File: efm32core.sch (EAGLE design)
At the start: 53 parts, among them U1 IP4220CZ6SSOT-6, U2 HC_05, U3 USD-SOCKETNEW, X1 48.0MHz, Y1 32.768kHz

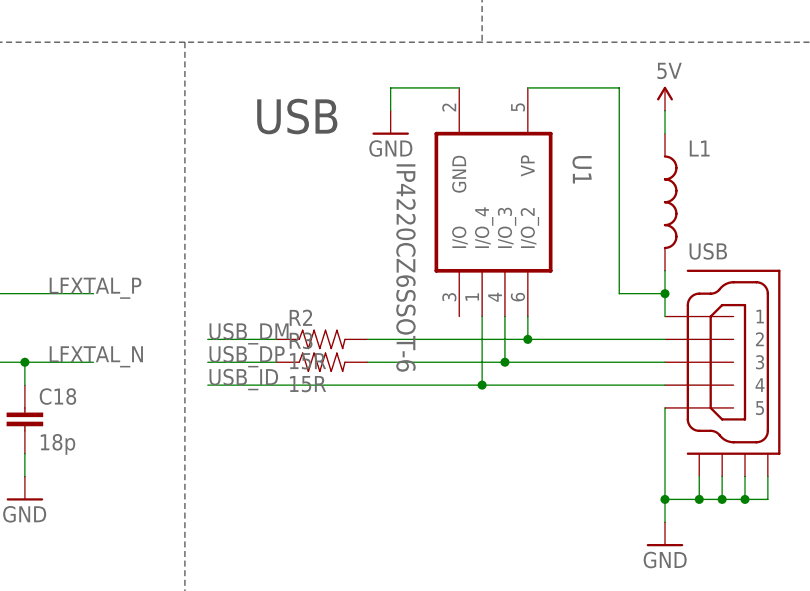
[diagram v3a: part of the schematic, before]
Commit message: update component name
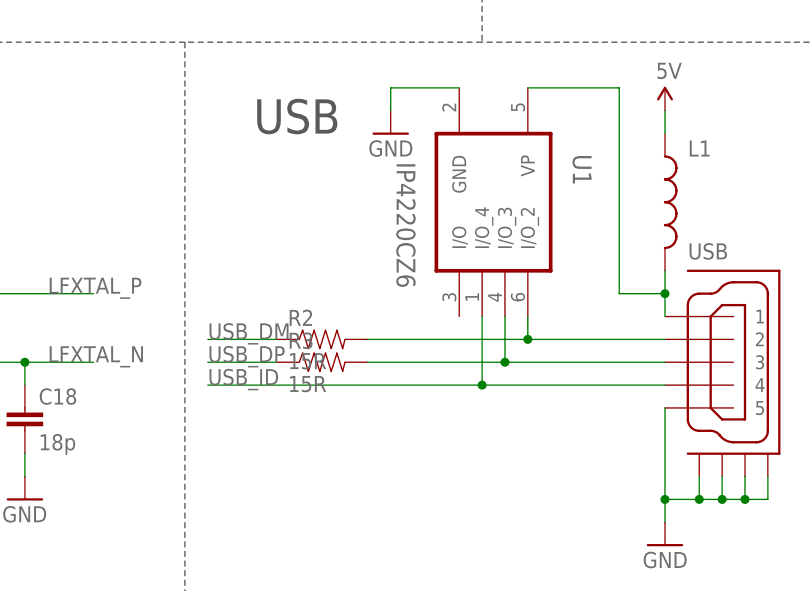
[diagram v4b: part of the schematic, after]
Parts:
- U1: value IP4220CZ6SSOT-6 -> IP4220CZ6
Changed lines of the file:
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@@
 <grid distance="0.1" unitdist="inch" unit="inch" style="lines" multiple="1" display="yes" altdistance="0.01" altunitdist="inch" altunit="inch"/>
 <layers>
-<layer number="1" name="Top" color="4" fill="1" visible="yes" active="no"/>
-<layer number="16" name="Bottom" color="1" fill="1" visible="yes" active="no"/>
-<layer number="17" name="Pads" color="2" fill="1" visible="yes" active="no"/>
-<layer number="18" name="Vias" color="2" fill="1" visible="yes" active="no"/>
-<layer number="19" name="Unrouted" color="6" fill="1" visible="yes" active="no"/>
-<layer number="20" name="Dimension" color="15" fill="1" visible="yes" active="no"/>
-<layer number="21" name="tPlace" color="7" fill="1" visible="yes" active="no"/>
-<layer number="22" name="bPlace" color="7" fill="1" visible="yes" active="no"/>
-<layer number="23" name="tOrigins" color="15" fill="1" visible="yes" active="no"/>
-<layer number="24" name="bOrigins" color="15" fill="1" visible="yes" active="no"/>
-<layer number="25" name="tNames" color="7" fill="1" visible="yes" active="no"/>
-<layer number="26" name="bNames" color="7" fill="1" visible="yes" active="no"/>
-<layer number="27" name="tValues" color="7" fill="1" visible="yes" active="no"/>
-<layer number="28" name="bValues" color="7" fill="1" visible="yes" active="no"/>
+<layer number="1" name="Top" color="4" fill="1" visible="no" active="no"/>
+<layer number="16" name="Bottom" color="1" fill="1" visible="no" active="no"/>
+<layer number="17" name="Pads" color="2" fill="1" visible="no" active="no"/>
+<layer number="18" name="Vias" color="2" fill="1" visible="no" active="no"/>
+<layer number="19" name="Unrouted" color="6" fill="1" visible="no" active="no"/>
+<layer number="20" name="Dimension" color="15" fill="1" visible="no" active="no"/>
+<layer number="21" name="tPlace" color="7" fill="1" visible="no" active="no"/>
+<layer number="22" name="bPlace" color="7" fill="1" visible="no" active="no"/>
+<layer number="23" name="tOrigins" color="15" fill="1" visible="no" active="no"/>
+<layer number="24" name="bOrigins" color="15" fill="1" visible="no" active="no"/>
+<layer number="25" name="tNames" color="7" fill="1" visible="no" active="no"/>
+<layer number="26" name="bNames" color="7" fill="1" visible="no" active="no"/>
+<layer number="27" name="tValues" color="7" fill="1" visible="no" active="no"/>
+<layer number="28" name="bValues" color="7" fill="1" visible="no" active="no"/>
 <layer number="29" name="tStop" color="7" fill="3" visible="no" active="no"/>
 <layer number="30" name="bStop" color="7" fill="6" visible="no" active="no"/>
@@
 <layer number="35" name="tGlue" color="7" fill="4" visible="no" active="no"/>
 <layer number="36" name="bGlue" color="7" fill="5" visible="no" active="no"/>
-<layer number="37" name="tTest" color="7" fill="1" visible="yes" active="no"/>
-<layer number="38" name="bTest" color="7" fill="1" visible="yes" active="no"/>
+<layer number="37" name="tTest" color="7" fill="1" visible="no" active="no"/>
+<layer number="38" name="bTest" color="7" fill="1" visible="no" active="no"/>
 <layer number="39" name="tKeepout" color="4" fill="11" visible="no" active="no"/>
 <layer number="40" name="bKeepout" color="1" fill="11" visible="no" active="no"/>
@@
 <layer number="44" name="Drills" color="7" fill="1" visible="no" active="no"/>
 <layer number="45" name="Holes" color="7" fill="1" visible="no" active="no"/>
-<layer number="46" name="Milling" color="3" fill="1" visible="yes" active="no"/>
-<layer number="47" name="Measures" color="7" fill="1" visible="yes" active="no"/>
-<layer number="48" name="Document" color="7" fill="1" visible="yes" active="no"/>
-<layer number="49" name="Reference" color="7" fill="1" visible="yes" active="no"/>
-<layer number="50" name="dxf" color="7" fill="1" visible="yes" active="no"/>
-<layer number="51" name="tDocu" color="14" fill="1" visible="yes" active="no"/>
-<layer number="52" name="bDocu" color="6" fill="1" visible="yes" active="no"/>
-<layer number="53" name="tGND_GNDA" color="7" fill="9" visible="yes" active="no"/>
-<layer number="54" name="bGND_GNDA" color="1" fill="9" visible="yes" active="no"/>
-<layer number="56" name="wert" color="7" fill="1" visible="yes" active="no"/>
-<layer number="57" name="tCAD" color="7" fill="1" visible="yes" active="no"/>
-<layer number="58" name="bCAD" color="7" fill="1" visible="yes" active="no"/>
+<layer number="46" name="Milling" color="3" fill="1" visible="no" active="no"/>
+<layer number="47" name="Measures" color="7" fill="1" visible="no" active="no"/>
+<layer number="48" name="Document" color="7" fill="1" visible="no" active="no"/>
+<layer number="49" name="Reference" color="7" fill="1" visible="no" active="no"/>
+<layer number="50" name="dxf" color="7" fill="1" visible="no" active="no"/>
+<layer number="51" name="tDocu" color="14" fill="1" visible="no" active="no"/>
+<layer number="52" name="bDocu" color="6" fill="1" visible="no" active="no"/>
+<layer number="53" name="tGND_GNDA" color="7" fill="9" visible="no" active="no"/>
+<layer number="54" name="bGND_GNDA" color="1" fill="9" visible="no" active="no"/>
+<layer number="56" name="wert" color="7" fill="1" visible="no" active="no"/>
+<layer number="57" name="tCAD" color="7" fill="1" visible="no" active="no"/>
+<layer number="58" name="bCAD" color="7" fill="1" visible="no" active="no"/>
 <layer number="91" name="Nets" color="2" fill="1" visible="yes" active="yes"/>
 <layer number="92" name="Busses" color="1" fill="1" visible="yes" active="yes"/>
@@
 <part name="L1" library="SparkFun-Passives" deviceset="INDUCTOR" device="0603"/>
 <part name="5V5" library="SparkFun-Aesthetics" deviceset="5V" device=""/>
-<part name="U1" library="FT232H-basic" deviceset="IP4220CZ6" device="SSOT-6"/>
+<part name="U1" library="FT232H-basic" deviceset="IP4220CZ6" device="SSOT-6" value="IP4220CZ6"/>
 <part name="GND9" library="SparkFun-Aesthetics" deviceset="GND" device=""/>
 <part name="R2" library="SparkFun-Resistors" deviceset="100-1%" device="" value="15R"/>

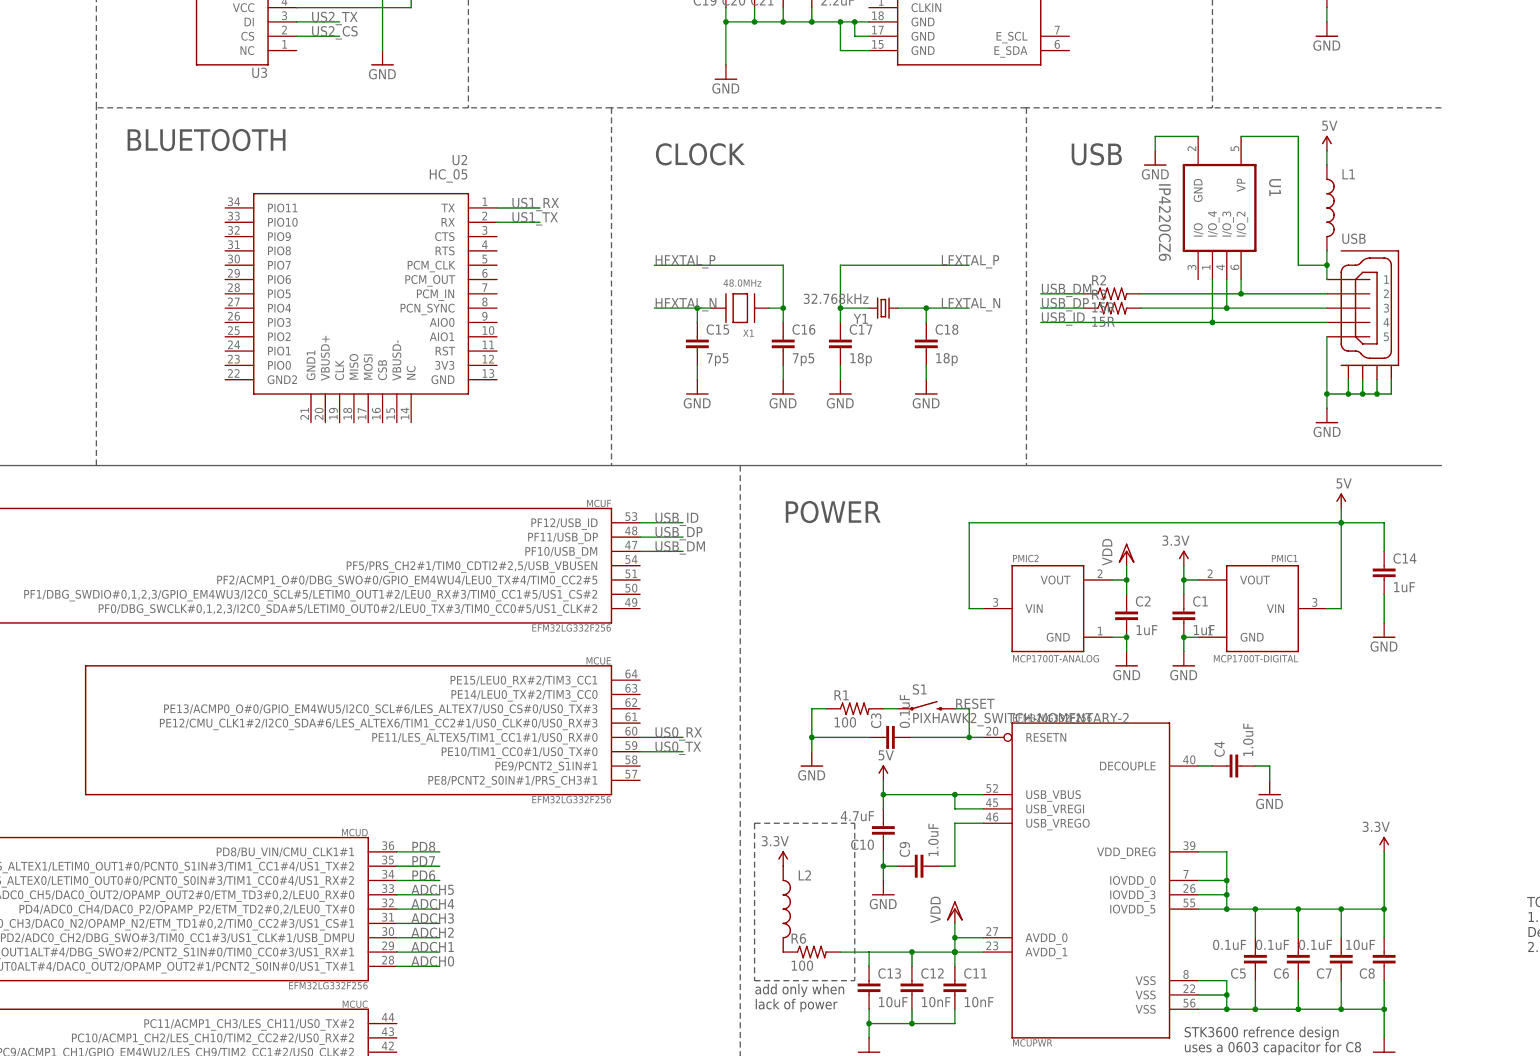
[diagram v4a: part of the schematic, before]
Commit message: do some fixes and updates
1. Fix L1 option.
2. Add a cap for bluetooth module.
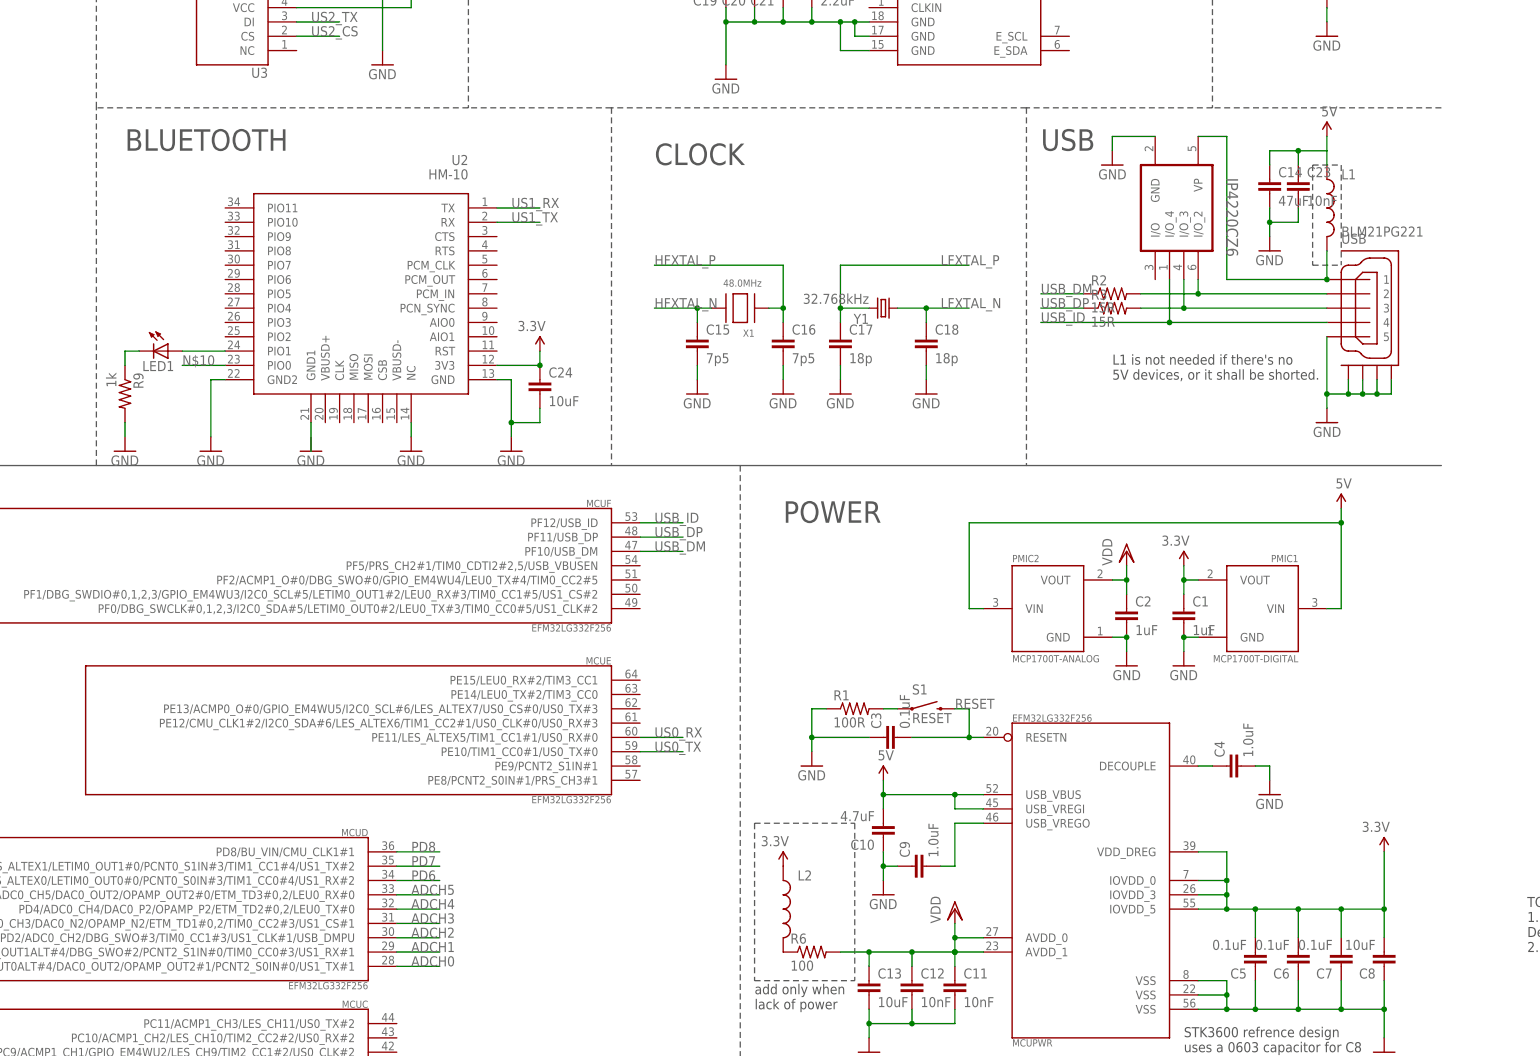
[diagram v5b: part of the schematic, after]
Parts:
- removed U1: IP4220CZ6, FT232H-basic:IP4220CZ6SSOT-6
- added C23: 10nF, SparkFun-Capacitors:10NF/10000PF-50V-10%(0603)
- added C24: 10uF, SparkFun-Capacitors:10UF-6.3V-20%(1206)
- added IP4220CZ6: IP4220CZ6SSOT-6, FT232H-basic:IP4220CZ6SSOT-6
- added LED1: (no value), adafruit:LEDCHIPLED_0603
- added R9: 1k, SparkFun-Resistors:100OHM1/10W1%(0603)
- C14: value 1uF -> 47uF
- L1: value (none) -> BLM21PG221; device SparkFun-Passives:INDUCTOR0603 -> SparkFun-Passives:INDUCTOR0805
- R1: value 100 -> 100R
- S1: value PIXHAWK2_SWITCH-MOMENTARY-2 -> RESET
- U2: value HC_05 -> HM-10
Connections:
- new net N$10: U2.PIO0
- new net N$16: U2.GND1
- new net N$2: LED1.A, U2.PIO1
- new net N$5: LED1.C, R9.1
- net 1: now also IP4220CZ6.VP; no longer U1.VP
- net 3.3V: now also C24.1, U2.3V3
- net 5V: now also C23.1
- net GND: now also C23.2, C24.2, IP4220CZ6.GND, R9.2, U2.GND, U2.GND2, U2.NC; no longer U1.GND
- net N$13: now also IP4220CZ6.I/O_3; no longer U1.I/O_3
- net N$14: now also IP4220CZ6.I/O_2; no longer U1.I/O_2
- net USB_ID: now also IP4220CZ6.I/O_4; no longer U1.I/O_4
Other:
- note added: "L1 is not needed if there's no 5V devices, or it shall be shorted."
- moved on the sheet: C14
